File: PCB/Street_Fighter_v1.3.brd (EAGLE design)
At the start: 59.9 x 77.5 mm, 73 parts, among them J1 FEMALE 2x3, Q1 BSS138, Q10 BSS138, Q2 BSS138, Q3 FQP30N06L, Q4 BSS138, Q5 BSS138, Q6 BSS138, Q7 BSS138, Q9 BSS138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

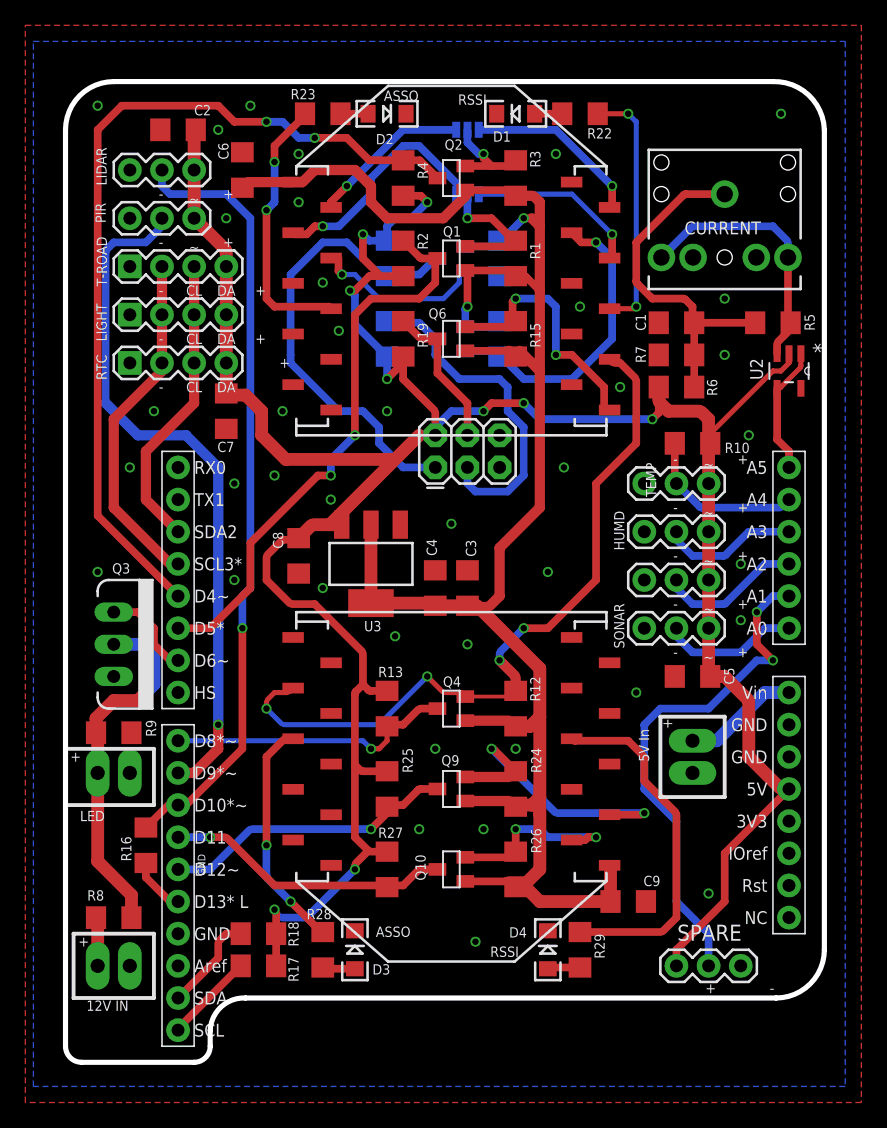
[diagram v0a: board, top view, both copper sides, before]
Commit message: StreetFighter v1.3 board - Fixed bad pin assignments for SoftSerial
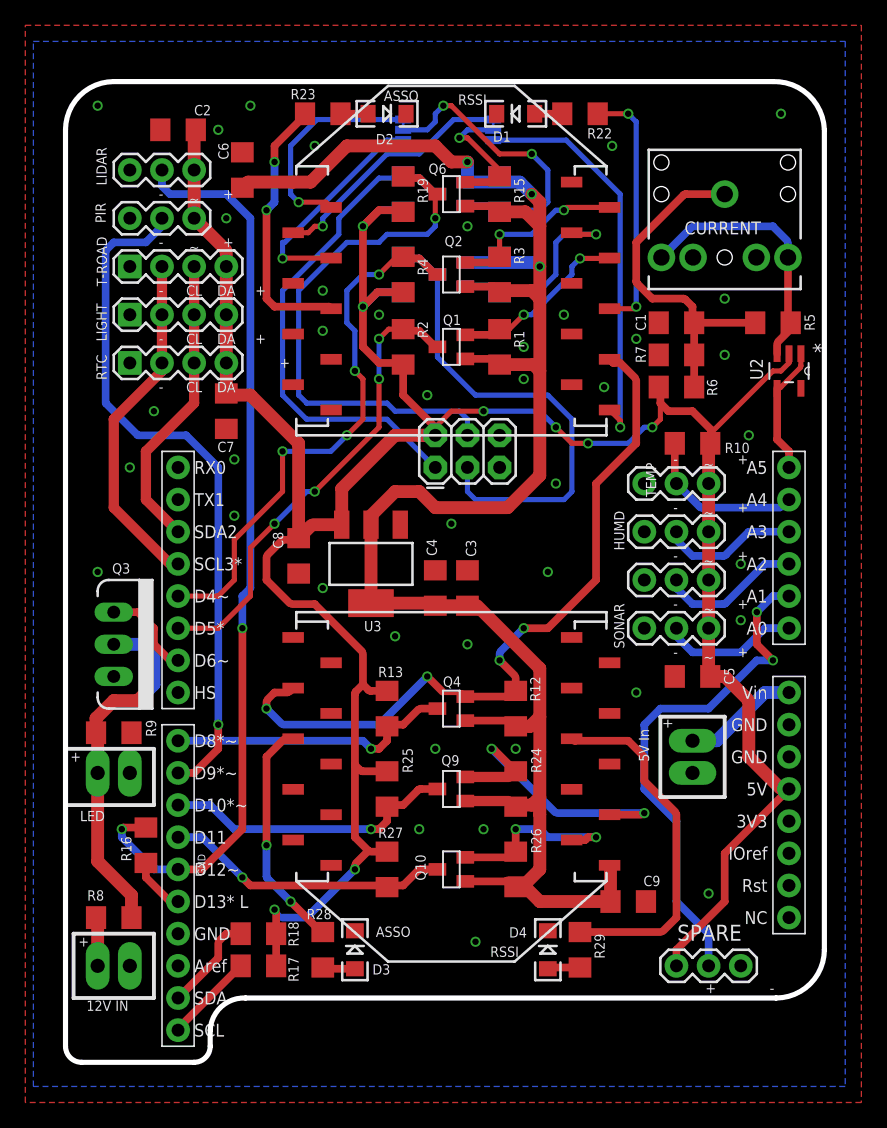
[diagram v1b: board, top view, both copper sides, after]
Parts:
- XBEE-IN, XBEE-OUT: value (none) -> JUMPER-PAD-3-2OF3_NC_BY_TRACE_SMALL; device SparkFun-Retired:SJ_3 -> SparkFun-Passives:PAD-JUMPER-3-2OF3_NC_BY_TRACE_YES_SILK_FULL_BOX
- moved R15 11.5 mm to (34.3, 68.6)
- moved Q6 11.4 mm to (30.5, 68.6)
- moved R19 11.4 mm to (26.7, 68.6)
- moved R3 7.73 mm to (34.3, 62.2)
- moved Q2 7.62 mm to (30.5, 62.2)
- moved R4 7.62 mm to (26.7, 62.2)
- moved R1 7.10 mm to (34.3, 56.5)
- moved Q1 6.98 mm to (30.5, 56.5)
- moved R2 6.98 mm to (26.7, 56.5)
- moved XBEE-IN 5.47 mm to (33.8, 73.7), turned to 90 degrees
- moved R14 5.24 mm to (26.7, 68.6), turned to 270 degrees
- moved R21 5.24 mm to (26.7, 62.2)
- moved Q5 5.08 mm to (30.5, 68.6)
- moved Q7 5.08 mm to (30.5, 62.2)
- moved R11 5.08 mm to (34.3, 68.6)
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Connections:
- net RX-XB renamed SPI-ATTN
- net TX-XB renamed SPI-SS
- net XB-SCK renamed 3V-SCK
- removed net XB-RX3V: Q2.2, R3.1, XBEE-OUT.2
- removed net XB-TX3V: Q1.2, R1.1, XBEE-IN.2
- new net 3V-MISO: Q5.2, R11.1, XBEE-OUT.2
- new net 3V-MOSI: Q6.2, R15.1, XBEE-IN.2
- net LIDAR-PWM: now also U1.12; no longer U1.10
- net TX-XB2: now also U1.10; no longer U1.12
- net XB-ATTN: now also Q2.2, R3.1; no longer XBEE-OUT.1
- net XB-MISO: now also XBEE-OUT.1; no longer Q5.2, R11.1
- net XB-MOSI: now also XBEE-IN.1; no longer Q6.2, R15.1
- net XB-SS: now also Q1.2, R1.1; no longer XBEE-IN.1
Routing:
- net MOSI: track 11.9 -> 42.4 mm, vias 0 -> 1
- net 3V-MISO: track 0.00 -> 27.0 mm, vias 0 -> 2
- net SPI-ATTN: track 69.5 -> 43.7 mm, vias 2 -> 4
- net XB-TX3V: track 14.8 -> 0.00 mm, vias 1 -> 0
- net SCK: track 26.7 -> 38.9 mm
- net XB-MOSI: track 20.6 -> 31.9 mm, vias 2 -> 1
- net LIDAR-PWM: track 61.7 -> 72.3 mm, vias 1 -> 2
- net 3V-MOSI: track 0.00 -> 10.6 mm, vias 0 -> 1
- net +5V: track 241.2 -> 232.2 mm, vias 9 -> 8
- net 3V-SCK: track 24.9 -> 15.9 mm
- net SPI-SS: track 45.3 -> 37.2 mm, vias 2 -> 4
- net XB-RX3V: track 8.04 -> 0.00 mm, vias 1 -> 0
- net +3V3: track 160.1 -> 165.4 mm, vias 2 -> 3
- net XB-DOUT: track 12.7 -> 17.5 mm
- net MISO: track 36.9 -> 40.4 mm
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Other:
- board text added: "2016-05-19"
- board text removed: "2016-05-16"
